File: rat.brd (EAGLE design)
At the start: 102.8 x 104.1 mm, 66 parts, among them J1 B2B-PH-K-S(LF)(SN), J2 B2B-PH-K-S(LF)(SN), J3 PPTC041LFBN-RC, J4 PPTC081LFBN-RCCONN_PPTC081LFB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, Q1A SFH_313_FA-3/4, Q1B SFH_313_FA-3/4, Q1C SFH_313_FA-3/4, Q1D SFH_313_FA-3/4, Q2A Q2, Q2B Q2, Q2C Q2, Q2D Q2, U1 L293DD, U2 LD1117D33CTR, U3 STM32F205RGT6

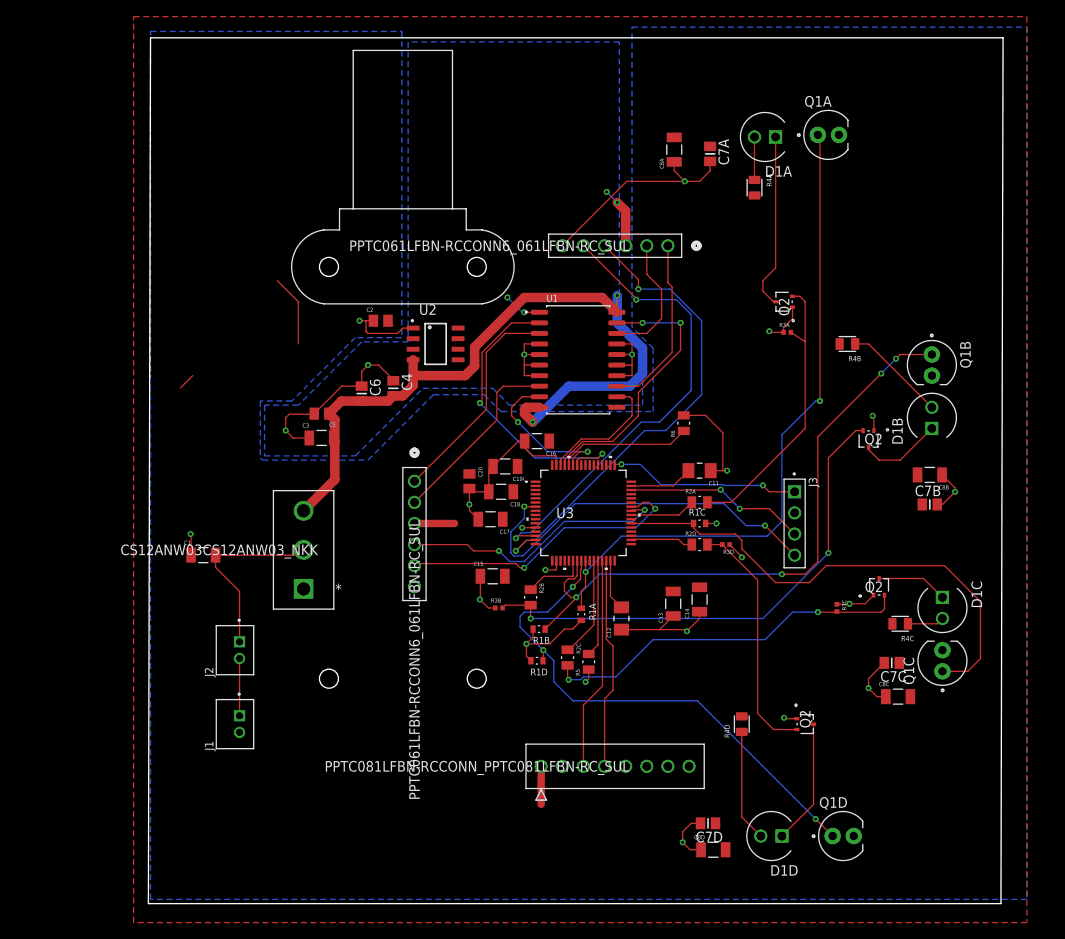
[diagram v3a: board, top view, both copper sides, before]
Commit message: First 6 Review-Required Changes Complete
Detailed in the "Team 27 PCB Review" Google Doc
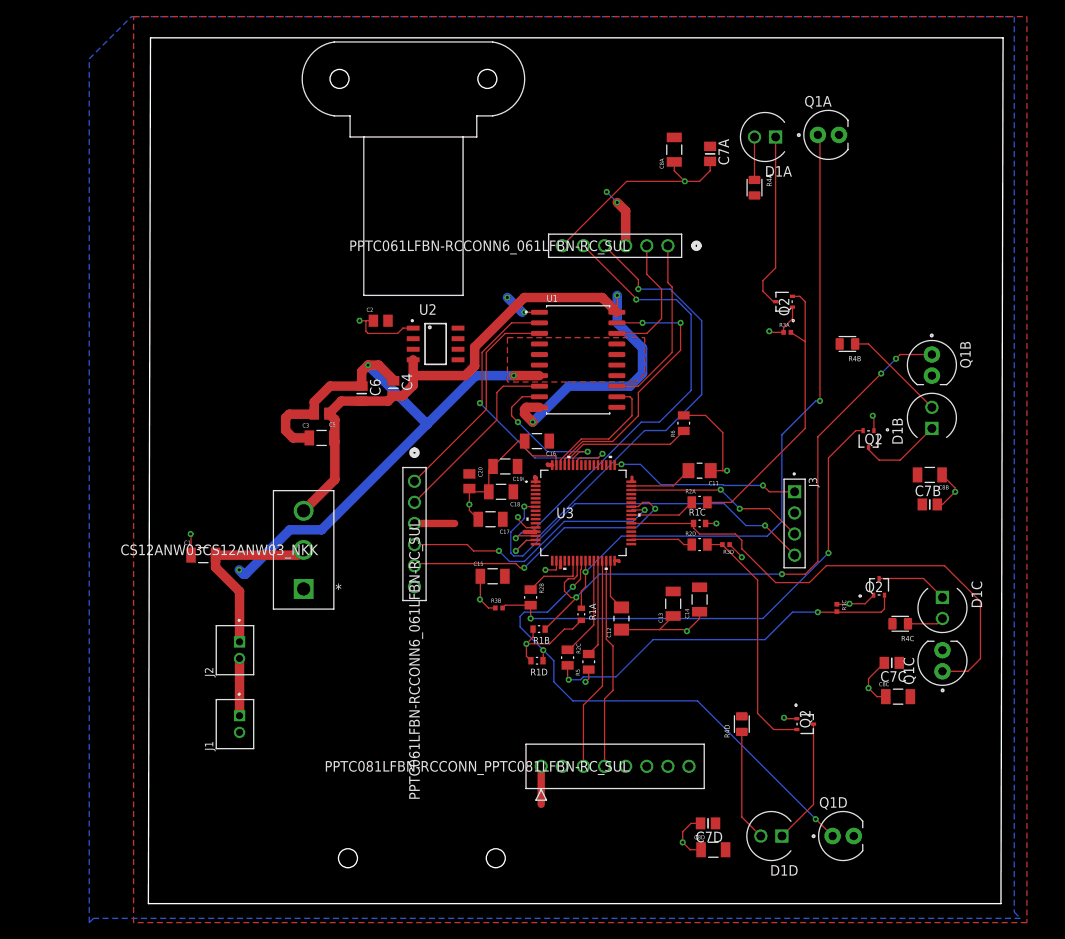
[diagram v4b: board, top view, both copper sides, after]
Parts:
- moved U$1 36.7 mm to (24.4, 27.7), turned to 90 degrees
- moved U$2 36.0 mm to (23.4, 64.3), turned to 270 degrees
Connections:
- net VCC: now also U2.3, U2.6, U2.7
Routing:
- net MGND: track 44.4 -> 79.3 mm, vias 4 -> 3
- net VCC: track 33.0 -> 26.1 mm
- net GND: track 141.6 -> 142.8 mm
- added copper zone on layer 1, net MGND
- removed copper zone on layer 16, net MGND

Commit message: Most of Crucial Changes Made
Still need to fix rest of trace sizes, make sure all decoupling capacitors are near the correct components, and switch out the incorrect MOSFET for the correct part.
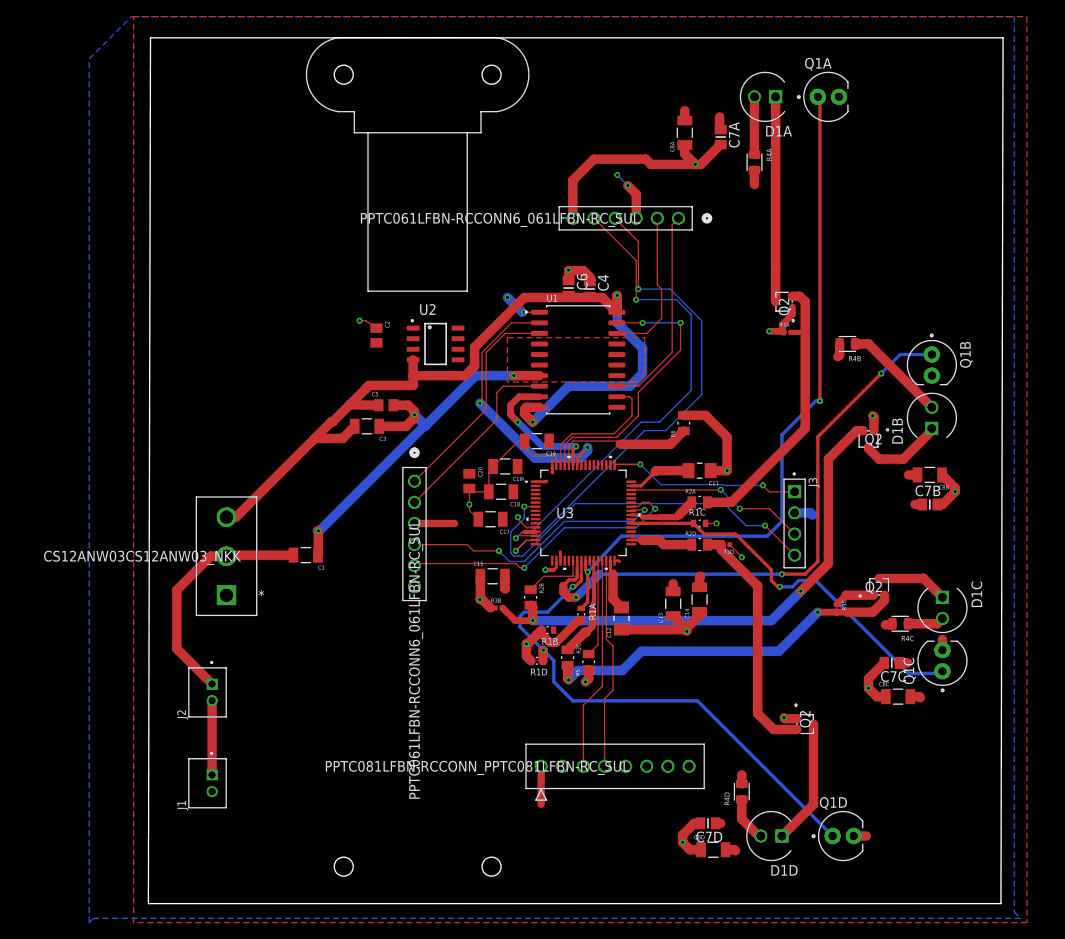
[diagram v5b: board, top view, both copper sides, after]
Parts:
- moved C6 27.9 mm to (47.8, 67.7)
- moved C4 26.5 mm to (50.3, 67.6)
- moved C1 12.3 mm to (16.1, 35.6), turned to 180 degrees
- moved S1 9.30 mm to (6.60, 30.7)
- moved R4D 8.13 mm to (68.6, 7.11)
- moved J1 7.84 mm to (4.32, 8.13)
- moved C5 7.81 mm to (25.8, 53.6), turned to 0 degrees
- moved J2 6.06 mm to (4.32, 19.1)
- moved C3 5.64 mm to (23.5, 51.1), turned to 180 degrees
- moved D1A 4.83 mm to (71.4, 90.7)
- moved Q1A 4.57 mm to (79.0, 90.7)
- moved RIGHT 3.54 mm to (61.0, 76.1)
- moved R4A 3.05 mm to (70.1, 82.8)
- moved C7A 2.40 mm to (66.0, 85.9)
- moved C8A 2.40 mm to (61.7, 86.4)
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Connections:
- net GND: now also C4.1, C6.1
- net MGND: no longer C4.1, C6.1
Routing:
- net MGND: track 79.3 -> 44.7 mm, vias 3 -> 2
- net VCC: track 26.1 -> 46.3 mm
- net PC7: track 60.6 -> 46.4 mm, vias 0 -> 1
- net VBAT: track 91.3 -> 103.7 mm
- net N$18: track 13.5 -> 5.49 mm
- net N$2: track 22.5 -> 28.8 mm
- net PA7: track 75.5 -> 70.3 mm, vias 4 -> 3
- net PC5: track 80.9 -> 85.5 mm
- net N$7: track 21.2 -> 24.9 mm
- net N$5: track 21.4 -> 24.8 mm
- net PA1: track 58.0 -> 60.8 mm
- net PA0: track 56.5 -> 59.3 mm
- net N$6: track 15.6 -> 18.4 mm
- net PB6: track 36.2 -> 33.7 mm
- net N$1: track 6.89 -> 8.92 mm
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
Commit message: DRC Cleared
Necessary changes: make sure decoupling capacitors are near components, adjust power trace sizes
Suggested Changes: clarify silkscreen, narrow board, round pcb corners
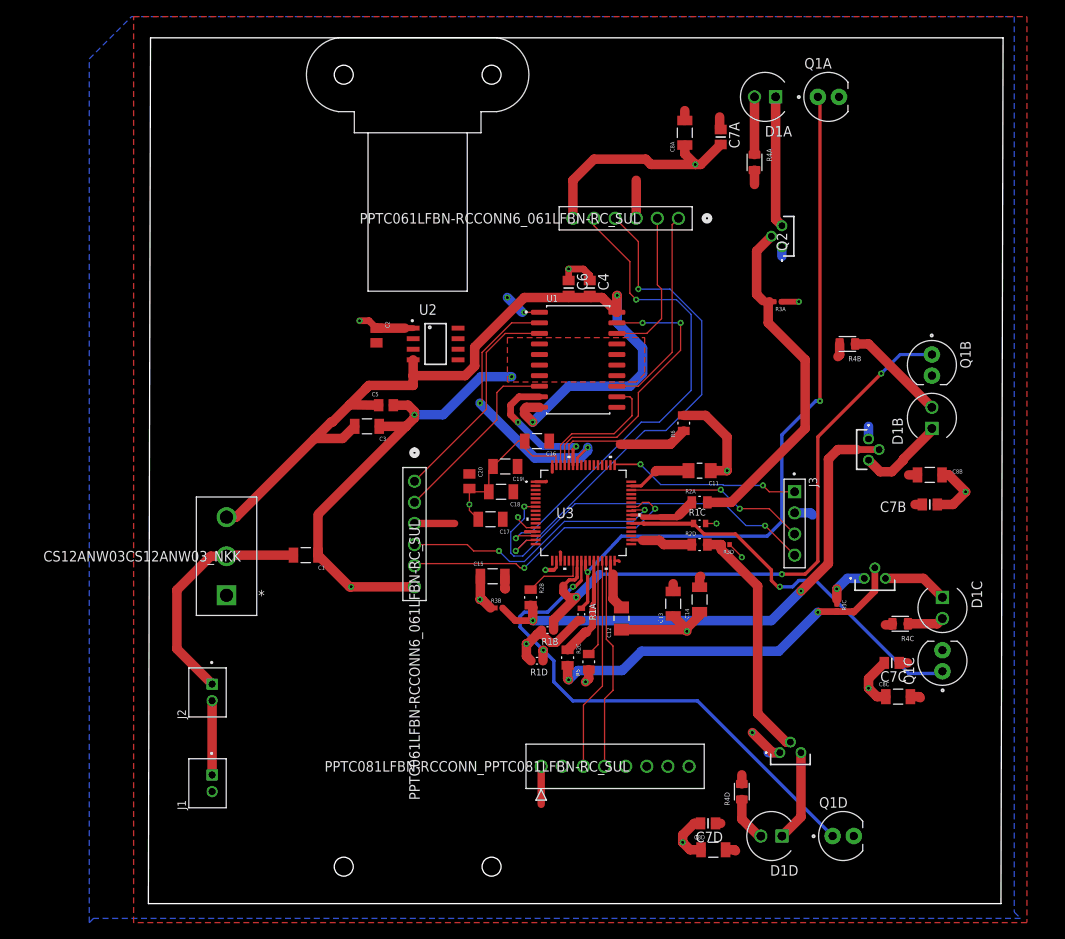
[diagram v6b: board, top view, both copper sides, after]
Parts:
- Q2A, Q2B, Q2C, Q2D: device 2022-01-23_01-58-16_Library:TRANS_RZF013P_ROM -> SamacSys_Parts:PF5102
- moved Q2A 6.61 mm to (73.4, 72.6), turned to 270 degrees
- moved Q2D 4.59 mm to (73.2, 11.8), turned to 180 degrees
- moved R3A 3.86 mm to (72.9, 66.0), turned to 180 degrees
- moved Q2C 2.05 mm to (83.3, 32.8), turned to 180 degrees
- moved C4 0.13 mm to (50.3, 67.7)
- turned Q2B to 90 degrees
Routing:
- net GND: track 144.6 -> 169.3 mm
- net N$7: track 24.9 -> 15.8 mm
- net N$8: track 34.2 -> 42.8 mm
- net MGND: track 44.7 -> 36.8 mm
- net PA7: track 70.3 -> 75.4 mm
- net VCC: track 46.3 -> 41.7 mm, vias 4 -> 2
- net N$16: track 15.0 -> 11.0 mm
- net N$10: track 44.4 -> 45.9 mm
- net N$9: track 8.57 -> 7.80 mm
- net N$14: track 63.1 -> 63.8 mm
- net N$13: track 9.96 -> 10.6 mm
- net VBAT: track 103.7 -> 104.2 mm
